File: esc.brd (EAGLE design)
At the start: 98.7 x 39.3 mm, 65 parts, among them IC1 78L05F, Q1 16 MHz, T1 IRFR1205, T2 IRFR1205, T3 IRFR1205, T4 IRFR1205, T5 IRFR1205, T6 IRFR1205, U1 ATMEGA48-20AU

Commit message: 4 Außenbohrungen und Shunt
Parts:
- R10: device resistor-power:AC01 -> resistor-power:CA5150
- moved R10 2.03 mm to (64.5, 5.08)
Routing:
- net N$8: track 67.8 -> 69.0 mm
- net SD_A: track 97.3 -> 96.2 mm
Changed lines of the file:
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@@
 <layer number="14" name="Route14" color="1" fill="6" visible="no" active="no"/>
 <layer number="15" name="Route15" color="4" fill="6" visible="no" active="no"/>
-<layer number="16" name="Bottom" color="1" fill="1" visible="no" active="yes"/>
+<layer number="16" name="Bottom" color="1" fill="1" visible="yes" active="yes"/>
 <layer number="17" name="Pads" color="2" fill="1" visible="yes" active="yes"/>
 <layer number="18" name="Vias" color="2" fill="1" visible="yes" active="yes"/>
-<layer number="19" name="Unrouted" color="6" fill="1" visible="no" active="yes"/>
+<layer number="19" name="Unrouted" color="6" fill="1" visible="yes" active="yes"/>
 <layer number="20" name="Dimension" color="15" fill="1" visible="yes" active="yes"/>
-<layer number="21" name="tPlace" color="7" fill="1" visible="no" active="yes"/>
+<layer number="21" name="tPlace" color="7" fill="1" visible="yes" active="yes"/>
 <layer number="22" name="bPlace" color="7" fill="1" visible="no" active="yes"/>
 <layer number="23" name="tOrigins" color="15" fill="1" visible="no" active="yes"/>
@@
 <element name="R9" library="rcl" package="R1206" value="680" x="57.15" y="12.065" rot="R90"/>
 <element name="C15" library="rcl" package="C1206" value="100nF" x="59.69" y="12.065" rot="R90"/>
-<element name="R10" library="resistor-power" package="AC01" value="" x="63.1825" y="6.6675" rot="R180">
-<attribute name="OC_NEWARK" value="unknown" x="63.1825" y="6.6675" size="1.778" layer="27" rot="R180" display="off"/>
-<attribute name="MPN" value="" x="63.1825" y="6.6675" size="1.778" layer="27" rot="R180" display="off"/>
-<attribute name="MF" value="" x="63.1825" y="6.6675" size="1.778" layer="27" rot="R180" display="off"/>
-<attribute name="OC_FARNELL" value="unknown" x="63.1825" y="6.6675" size="1.778" layer="27" rot="R180" display="off"/>
+<element name="R10" library="resistor-power" package="CA5150" value="" x="64.4525" y="5.08" rot="R180">
+<attribute name="OC_NEWARK" value="unknown" x="64.4525" y="5.08" size="1.778" layer="27" rot="R180" display="off"/>
+<attribute name="MPN" value="" x="64.4525" y="5.08" size="1.778" layer="27" rot="R180" display="off"/>
+<attribute name="MF" value="" x="64.4525" y="5.08" size="1.778" layer="27" rot="R180" display="off"/>
+<attribute name="OC_FARNELL" value="unknown" x="64.4525" y="5.08" size="1.778" layer="27" rot="R180" display="off"/>
 </element>
 <element name="R11" library="rcl" package="R1206" value="4k7" x="69.5325" y="8.255" rot="MR270"/>
@@
 <wire x1="6.0325" y1="23.8125" x2="5.3975" y2="23.8125" width="0.4064" layer="1"/>
 <wire x1="5.3975" y1="23.8125" x2="3.81" y2="25.4" width="0.4064" layer="1"/>
-<wire x1="3.81" y1="25.4" x2="3.81" y2="33.655" width="0.4064" layer="1"/>
+<wire x1="3.81" y1="25.4" x2="3.81" y2="31.75" width="0.4064" layer="1"/>
 <wire x1="71.823284375" y1="24.691971875" x2="73.1663125" y2="26.035" width="0.4064" layer="1"/>
 <wire x1="73.1663125" y1="26.035" x2="77.1525" y2="26.035" width="0.4064" layer="1"/>
 <wire x1="77.1525" y1="26.035" x2="77.7875" y2="26.9875" width="0.4064" layer="1"/>
 <via x="77.7875" y="26.9875" extent="1-16" drill="0.6"/>
-<via x="4.445" y="34.29" extent="1-16" drill="0.6"/>
-<wire x1="4.445" y1="34.29" x2="3.81" y2="33.655" width="0.4064" layer="1"/>
-<wire x1="69.85" y1="35.8775" x2="6.0325" y2="35.8775" width="0.4064" layer="16"/>
-<wire x1="6.0325" y1="35.8775" x2="4.445" y2="34.29" width="0.4064" layer="16"/>
+<via x="13.0175" y="35.8775" extent="1-16" drill="0.6"/>
+<wire x1="69.85" y1="35.8775" x2="13.0175" y2="35.8775" width="0.4064" layer="16"/>
 <wire x1="69.85" y1="35.8775" x2="77.7875" y2="27.94" width="0.4064" layer="16"/>
 <wire x1="77.7875" y1="27.94" x2="77.7875" y2="26.9875" width="0.4064" layer="16"/>
+<wire x1="3.81" y1="31.75" x2="7.9375" y2="35.8775" width="0.4064" layer="1"/>
+<wire x1="7.9375" y1="35.8775" x2="13.0175" y2="35.8775" width="0.4064" layer="1"/>
 </signal>
 <signal name="N$9">
@@
 <contactref element="R9" pad="1"/>
 <contactref element="R10" pad="2"/>
-<wire x1="54.2825" y1="6.6675" x2="54.2825" y2="5.3875" width="1.6764" layer="16"/>
 <wire x1="54.2825" y1="5.3875" x2="51.435" y2="3.81" width="1.6764" layer="16"/>
 <wire x1="51.435" y1="3.81" x2="44.45" y2="3.81" width="1.6764" layer="16"/>
-<wire x1="44.45" y1="3.81" x2="30.48" y2="3.81" width="1.6764" layer="16"/>
+<wire x1="44.45" y1="3.81" x2="41.91" y2="3.81" width="1.6764" layer="16"/>
+<wire x1="41.91" y1="3.81" x2="30.48" y2="3.81" width="1.6764" layer="16"/>
 <wire x1="30.48" y1="3.81" x2="15.24" y2="3.81" width="1.6764" layer="16"/>
 <via x="15.24" y="3.81" extent="1-16" drill="0.6"/>
@@
 <via x="44.45" y="5.08" extent="1-16" drill="0.6"/>
 <wire x1="44.45" y1="5.08" x2="44.45" y2="3.81" width="1.6764" layer="16"/>
-<wire x1="54.2825" y1="6.6675" x2="54.2925" y2="6.6575" width="1.6764" layer="16"/>
-<wire x1="54.2925" y1="6.6575" x2="54.2925" y2="8.5725" width="1.6764" layer="16"/>
 <via x="54.2925" y="8.5725" extent="1-16" drill="0.6"/>
 <wire x1="54.2925" y1="8.5725" x2="54.458" y2="10.643" width="0.8128" layer="1"/>
 <wire x1="54.458" y1="10.643" x2="57.15" y2="10.643" width="0.8128" layer="1"/>
+<wire x1="54.2925" y1="8.5725" x2="54.2825" y2="8.5725" width="1.27" layer="16"/>
+<wire x1="54.2825" y1="8.5725" x2="54.2825" y2="5.3875" width="1.27" layer="16"/>
+<wire x1="42.2275" y1="5.08" x2="41.91" y2="3.81" width="1.27" layer="16"/>
 </signal>
 <signal name="NULL_A">
@@
 <signal name="N$7">
 </signal>
+<signal name="N$23">
+<via x="2.54" y="36.83" extent="1-16" drill="2.8"/>
+</signal>
+<signal name="N$25">
+<via x="2.54" y="2.54" extent="1-16" drill="2.8"/>
+</signal>
+<signal name="N$26">
+<via x="96.2025" y="2.54" extent="1-16" drill="2.8"/>
+</signal>
+<signal name="N$27">
+<via x="96.2025" y="36.83" extent="1-16" drill="2.8"/>
+</signal>
 </signals>

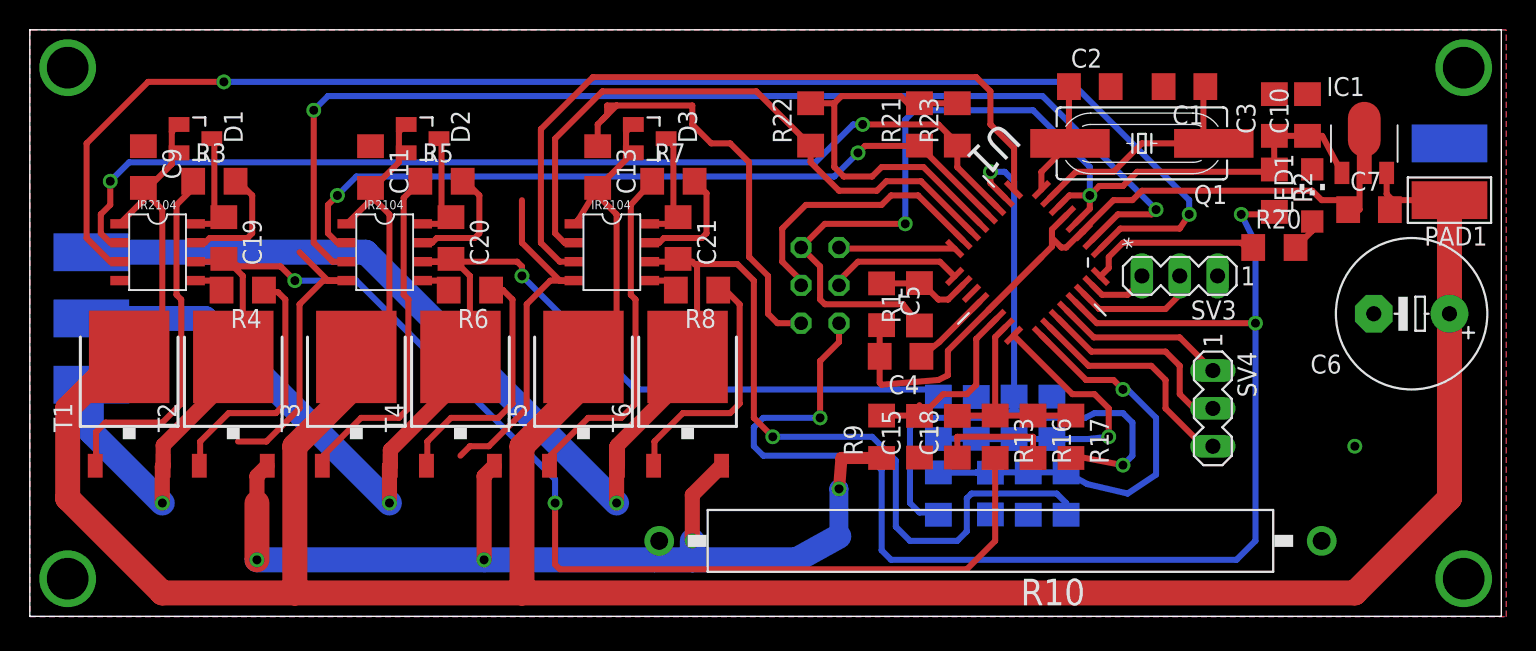
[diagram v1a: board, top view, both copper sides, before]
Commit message: Top optimierung für ätzen
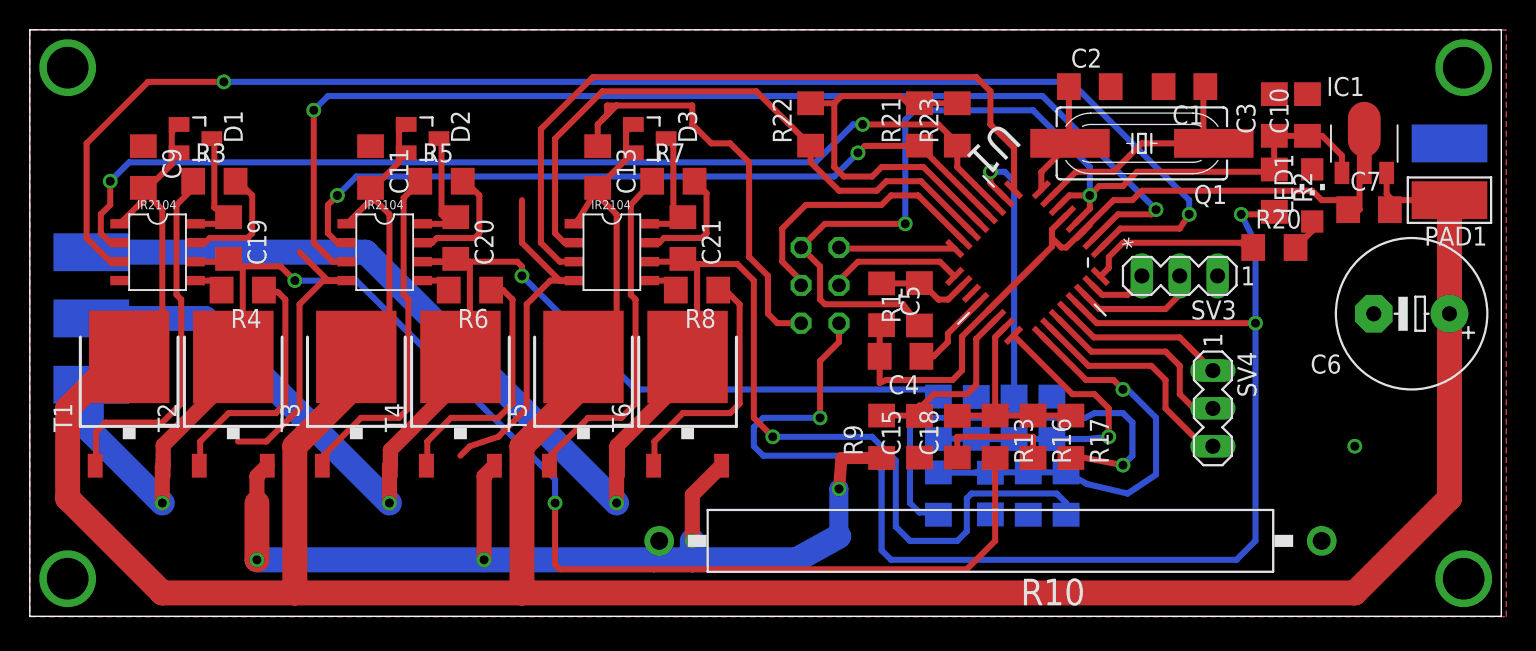
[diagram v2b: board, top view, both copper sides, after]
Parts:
- moved C19 0.32 mm to (13.3, 25.4)
- moved C20 0.32 mm to (28.6, 25.4)
- moved C21 0.32 mm to (43.8, 25.4)
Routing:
- net PHASE_A: track 102.2 -> 101.4 mm
- net N$9: track 7.95 -> 8.52 mm
- net N$18: track 7.69 -> 8.21 mm
- net N$10: track 7.69 -> 8.19 mm

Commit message: zweites gnd via
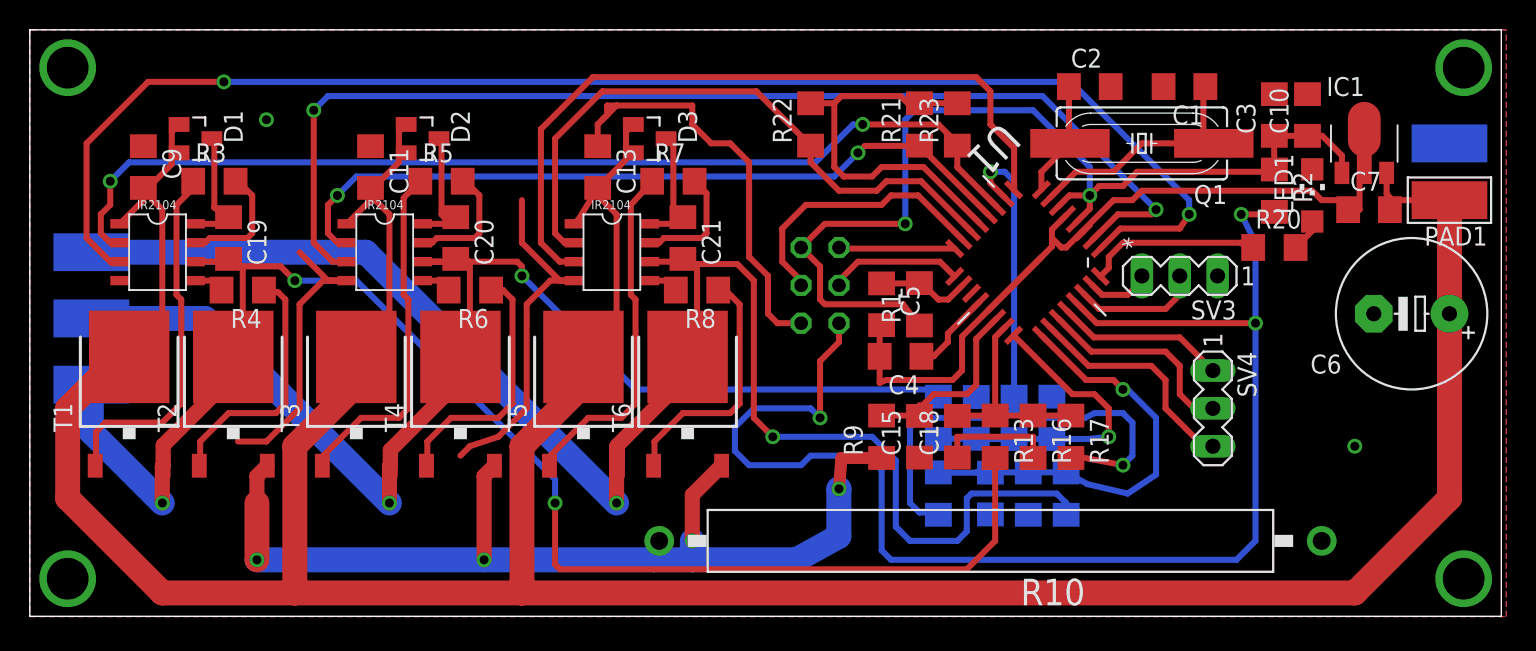
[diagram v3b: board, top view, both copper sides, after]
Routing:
- net RESET: track 91.0 -> 94.8 mm
- net GND: vias 1 -> 2
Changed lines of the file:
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@@
 <layer number="14" name="Route14" color="1" fill="6" visible="no" active="no"/>
 <layer number="15" name="Route15" color="4" fill="6" visible="no" active="no"/>
-<layer number="16" name="Bottom" color="1" fill="1" visible="no" active="yes"/>
+<layer number="16" name="Bottom" color="1" fill="1" visible="yes" active="yes"/>
 <layer number="17" name="Pads" color="2" fill="1" visible="yes" active="yes"/>
 <layer number="18" name="Vias" color="2" fill="1" visible="yes" active="yes"/>
 <layer number="19" name="Unrouted" color="6" fill="1" visible="yes" active="yes"/>
 <layer number="20" name="Dimension" color="15" fill="1" visible="yes" active="yes"/>
-<layer number="21" name="tPlace" color="7" fill="1" visible="yes" active="yes"/>
-<layer number="22" name="bPlace" color="7" fill="1" visible="no" active="yes"/>
-<layer number="23" name="tOrigins" color="15" fill="1" visible="yes" active="yes"/>
+<layer number="21" name="tPlace" color="7" fill="1" visible="no" active="yes"/>
+<layer number="22" name="bPlace" color="7" fill="1" visible="yes" active="yes"/>
+<layer number="23" name="tOrigins" color="15" fill="1" visible="no" active="yes"/>
 <layer number="24" name="bOrigins" color="15" fill="1" visible="no" active="yes"/>
 <layer number="25" name="tNames" color="7" fill="1" visible="no" active="yes"/>
@@
 <layer number="39" name="tKeepout" color="4" fill="11" visible="no" active="yes"/>
 <layer number="40" name="bKeepout" color="1" fill="11" visible="no" active="yes"/>
-<layer number="41" name="tRestrict" color="4" fill="10" visible="no" active="yes"/>
-<layer number="42" name="bRestrict" color="1" fill="10" visible="no" active="yes"/>
+<layer number="41" name="tRestrict" color="4" fill="10" visible="yes" active="yes"/>
+<layer number="42" name="bRestrict" color="1" fill="10" visible="yes" active="yes"/>
 <layer number="43" name="vRestrict" color="2" fill="10" visible="no" active="yes"/>
 <layer number="44" name="Drills" color="7" fill="1" visible="no" active="yes"/>
@@
 <layer number="49" name="Reference" color="7" fill="1" visible="no" active="yes"/>
 <layer number="50" name="dxf" color="7" fill="1" visible="no" active="yes"/>
-<layer number="51" name="tDocu" color="7" fill="1" visible="yes" active="yes"/>
-<layer number="52" name="bDocu" color="7" fill="1" visible="no" active="yes"/>
+<layer number="51" name="tDocu" color="7" fill="1" visible="no" active="yes"/>
+<layer number="52" name="bDocu" color="7" fill="1" visible="yes" active="yes"/>
 <layer number="91" name="Nets" color="2" fill="1" visible="no" active="no"/>
 <layer number="92" name="Busses" color="1" fill="1" visible="no" active="no"/>
@@
 <wire x1="86.0425" y1="28.575" x2="86.6775" y2="27.94" width="0.4064" layer="1"/>
 <wire x1="86.6775" y1="27.94" x2="87.63" y2="27.94" width="0.4064" layer="1"/>
+<via x="15.875" y="33.3375" extent="1-16" drill="0.6"/>
 </signal>
 <signal name="N$2">
@@
 <wire x1="54.458" y1="10.643" x2="57.15" y2="10.643" width="0.8128" layer="1"/>
 <wire x1="54.2925" y1="8.5725" x2="54.2825" y2="8.5725" width="1.27" layer="16"/>
-<wire x1="54.2825" y1="8.5725" x2="54.2825" y2="5.3875" width="1.27" layer="16"/>
 <wire x1="42.2275" y1="5.08" x2="41.91" y2="3.81" width="1.27" layer="16"/>
+<wire x1="54.2825" y1="5.3875" x2="54.2825" y2="8.5625" width="1.6764" layer="16"/>
+<wire x1="54.2825" y1="8.5625" x2="54.2925" y2="8.5725" width="1.6764" layer="16"/>
 </signal>
 <signal name="NULL_A">
@@
 <wire x1="83.5025" y1="26.67" x2="83.5025" y2="27.153" width="0.4064" layer="1"/>
 <via x="53.0225" y="13.335" extent="1-16" drill="0.6"/>
-<wire x1="53.0225" y1="13.335" x2="49.2125" y2="13.335" width="0.4064" layer="16"/>
-<wire x1="49.2125" y1="13.335" x2="48.5775" y2="12.7" width="0.4064" layer="16"/>
-<wire x1="48.5775" y1="12.7" x2="48.5775" y2="11.43" width="0.4064" layer="16"/>
-<wire x1="48.5775" y1="11.43" x2="49.2125" y2="10.795" width="0.4064" layer="16"/>
-<wire x1="49.2125" y1="10.795" x2="56.1975" y2="10.795" width="0.4064" layer="16"/>
+<wire x1="48.5775" y1="13.97" x2="47.3075" y2="12.7" width="0.4064" layer="16"/>
 <wire x1="56.1975" y1="10.795" x2="57.15" y2="9.8425" width="0.4064" layer="16"/>
 <wire x1="57.15" y1="9.8425" x2="57.15" y2="4.445" width="0.4064" layer="16"/>
@@
 <wire x1="54.2925" y1="18.415" x2="53.0225" y2="17.145" width="0.4064" layer="1"/>
 <wire x1="53.0225" y1="17.145" x2="53.0225" y2="13.335" width="0.4064" layer="1"/>
+<wire x1="47.3075" y1="12.7" x2="47.3075" y2="11.1125" width="0.4064" layer="16"/>
+<wire x1="47.3075" y1="11.1125" x2="48.26" y2="10.16" width="0.4064" layer="16"/>
+<wire x1="48.26" y1="10.16" x2="51.7525" y2="10.16" width="0.4064" layer="16"/>
+<wire x1="51.7525" y1="10.16" x2="52.3875" y2="10.795" width="0.4064" layer="16"/>
+<wire x1="52.3875" y1="10.795" x2="56.1975" y2="10.795" width="0.4064" layer="16"/>
+<wire x1="48.5775" y1="13.97" x2="52.3875" y2="13.97" width="0.4064" layer="16"/>
+<wire x1="52.3875" y1="13.97" x2="53.0225" y2="13.335" width="0.4064" layer="16"/>
 </signal>
 <signal name="N$7">
